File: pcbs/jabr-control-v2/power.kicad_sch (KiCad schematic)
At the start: 0 parts

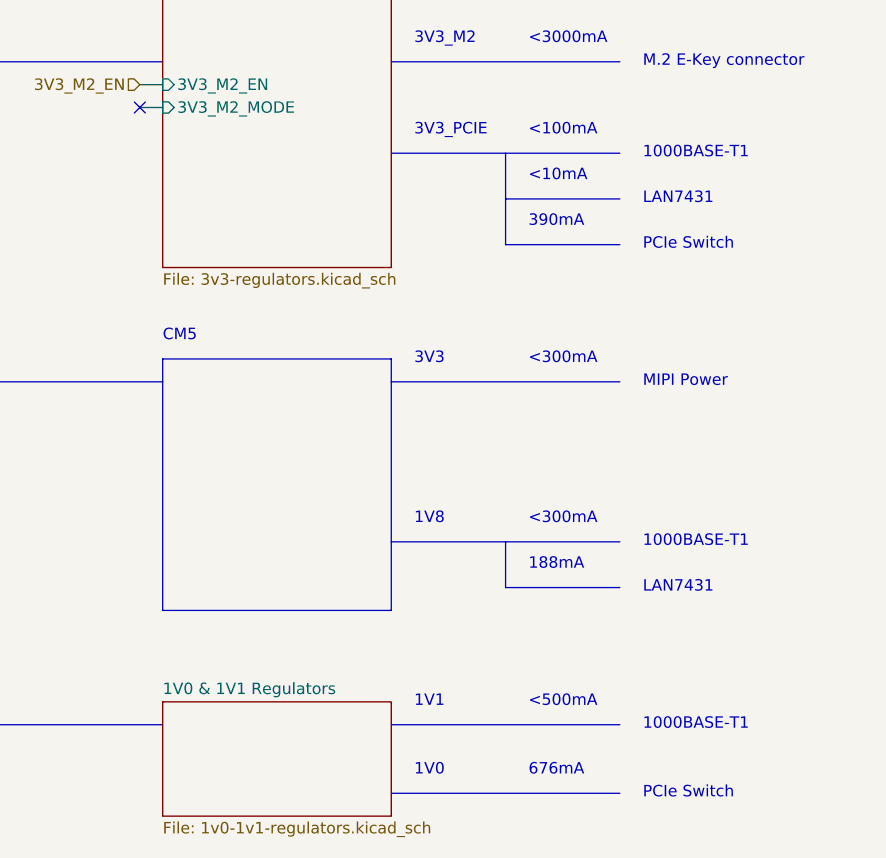
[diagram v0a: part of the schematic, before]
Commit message: PCI11010C Schematic sheet mostly done
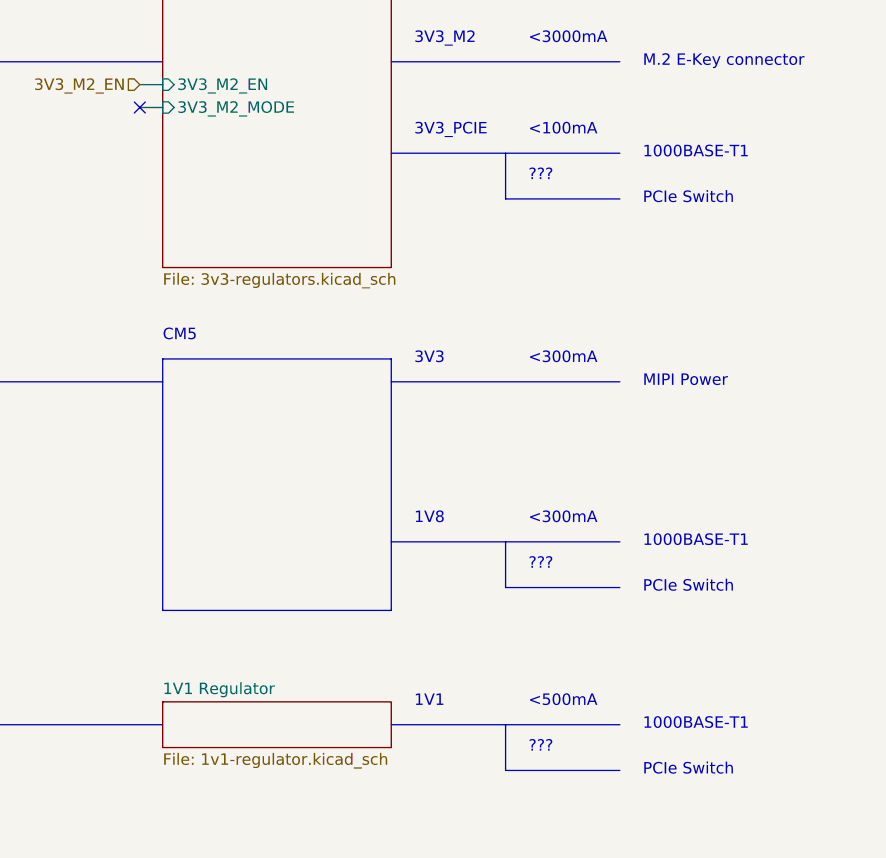
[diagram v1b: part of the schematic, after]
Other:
- sheet 1V0 & 1V1 Regulators renamed 1V1 Regulator
- sheet 1V1 Regulator: file 1v0-1v1-regulators.kicad_sch -> 1v1-regulator.kicad_sch
- note added: "???"
- note removed: "188mA"
- note removed: "1V0"
- note removed: "390mA"
- note removed: "676mA"
- note removed: "<10mA"
- note removed: "LAN7431"
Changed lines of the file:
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@@
 (kicad_sch
-	(version 20250114)
+	(version 20260306)
 	(generator "eeschema")
-	(generator_version "9.0")
+	(generator_version "10.0")
 	(paper "A4")
 	(rectangle
@@
 	(text "PCIe Switch"
 		(exclude_from_sim no)
-		(at 226.06 83.82 0)
-		(effects
-			(font
-				(size 1.27 1.27)
-			)
-			(justify left)
-		)
-	)
-	(text "676mA"
-		(exclude_from_sim no)
-		(at 213.36 142.24 0)
+		(at 226.06 78.74 0)
 		(effects
 			(font
@@
 		)
 	)
-	(text "LAN7431"
+	(text "PCIe Switch"
 		(exclude_from_sim no)
 		(at 226.06 121.92 0)
@@
 		)
 	)
-	(text "188mA"
+	(text "???"
 		(exclude_from_sim no)
 		(at 213.36 119.38 0)
@@
 		)
 	)
-	(text "LAN7431"
-		(exclude_from_sim no)
-		(at 226.06 78.74 0)
+	(text "???"
+		(exclude_from_sim no)
+		(at 213.36 139.7 0)
 		(effects
 			(font
@@
 		)
 	)
-	(text "<10mA"
+	(text "VIN (12V-24V)"
+		(exclude_from_sim no)
+		(at 86.36 43.18 0)
+		(effects
+			(font
+				(size 1.27 1.27)
+			)
+			(justify left)
+		)
+	)
+	(text "<500mA"
+		(exclude_from_sim no)
+		(at 213.36 134.62 0)
+		(effects
+			(font
+				(size 1.27 1.27)
+			)
+			(justify left)
+		)
+	)
+	(text "1V8"
+		(exclude_from_sim no)
+		(at 200.66 114.3 0)
+		(effects
+			(font
+				(size 1.27 1.27)
+			)
+			(justify left)
+		)
+	)
+	(text "<3000mA"
+		(exclude_from_sim no)
+		(at 213.36 60.96 0)
+		(effects
+			(font
+				(size 1.27 1.27)
+			)
+			(justify left)
+		)
+	)
+	(text "1000BASE-T1"
+		(exclude_from_sim no)
+		(at 226.06 73.66 0)
+		(effects
+			(font
+				(size 1.27 1.27)
+			)
+			(justify left)
+		)
+	)
+	(text "<300mA"
+		(exclude_from_sim no)
+		(at 213.36 114.3 0)
+		(effects
+			(font
+				(size 1.27 1.27)
+			)
+			(justify left)
+		)
+	)
+	(text "1000BASE-T1"
+		(exclude_from_sim no)
+		(at 226.06 137.16 0)
+		(effects
+			(font
+				(size 1.27 1.27)
+			)
+			(justify left)
+		)
+	)
+	(text "PCIe Switch"
+		(exclude_from_sim no)
+		(at 226.06 142.24 0)
+		(effects
+			(font
+				(size 1.27 1.27)
+			)
+			(justify left)
+		)
+	)
+	(text "CM5 VBAT"
+		(exclude_from_sim no)
+		(at 226.06 50.8 0)
+		(effects
+			(font
+				(size 1.27 1.27)
+			)
+			(justify left)
+		)
+	)
+	(text "3V3_AON"
+		(exclude_from_sim no)
+		(at 200.66 43.18 0)
+		(effects
+			(font
+				(size 1.27 1.27)
+			)
+			(justify left)
+		)
+	)
+	(text "???"
 		(exclude_from_sim no)
 		(at 213.36 76.2 0)
-		(effects
-			(font
-				(size 1.27 1.27)
-			)
-			(justify left)
-		)
-	)
-	(text "VIN (12V-24V)"
-		(exclude_from_sim no)
-		(at 86.36 43.18 0)
-		(effects
-			(font
-				(size 1.27 1.27)
-			)
-			(justify left)
-		)
-	)
-	(text "<500mA"
-		(exclude_from_sim no)
-		(at 213.36 134.62 0)
-		(effects
-			(font
-				(size 1.27 1.27)
-			)
-			(justify left)
-		)
-	)
-	(text "1V8"
-		(exclude_from_sim no)
-		(at 200.66 114.3 0)
-		(effects
-			(font
-				(size 1.27 1.27)
-			)
-			(justify left)
-		)
-	)
-	(text "<3000mA"
-		(exclude_from_sim no)
-		(at 213.36 60.96 0)
-		(effects
-			(font
-				(size 1.27 1.27)
-			)
-			(justify left)
-		)
-	)
-	(text "1000BASE-T1"
-		(exclude_from_sim no)
-		(at 226.06 73.66 0)
-		(effects
-			(font
-				(size 1.27 1.27)
-			)
-			(justify left)
-		)
-	)
-	(text "<300mA"
-		(exclude_from_sim no)
-		(at 213.36 114.3 0)
-		(effects
-			(font
-				(size 1.27 1.27)
-			)
-			(justify left)
-		)
-	)
-	(text "1000BASE-T1"
-		(exclude_from_sim no)
-		(at 226.06 137.16 0)
-		(effects
-			(font
-				(size 1.27 1.27)
-			)
-			(justify left)
-		)
-	)
-	(text "PCIe Switch"
-		(exclude_from_sim no)
-		(at 226.06 144.78 0)
-		(effects
-			(font
-				(size 1.27 1.27)
-			)
-			(justify left)
-		)
-	)
-	(text "CM5 VBAT"
-		(exclude_from_sim no)
-		(at 226.06 50.8 0)
-		(effects
-			(font
-				(size 1.27 1.27)
-			)
-			(justify left)
-		)
-	)
-	(text "3V3_AON"
-		(exclude_from_sim no)
-		(at 200.66 43.18 0)
-		(effects
-			(font
-				(size 1.27 1.27)
-			)
-			(justify left)
-		)
-	)
-	(text "1V0"
-		(exclude_from_sim no)
-		(at 200.66 142.24 0)
-		(effects
-			(font
-				(size 1.27 1.27)
-			)
-			(justify left)
-		)
-	)
-	(text "390mA"
-		(exclude_from_sim no)
-		(at 213.36 81.28 0)
 		(effects
 			(font
@@
 	(polyline
 		(pts
-			(xy 210.82 78.74) (xy 210.82 83.82)
+			(xy 210.82 78.74) (xy 210.82 78.74)
 		)
 		(stroke
@@
 	(polyline
 		(pts
-			(xy 223.52 83.82) (xy 210.82 83.82)
-		)
-		(stroke
-			(width 0)
-			(type default)
-		)
-	)
-	(polyline
-		(pts
 			(xy 223.52 78.74) (xy 210.82 78.74)
 		)
@@
 	(polyline
 		(pts
+			(xy 210.82 137.16) (xy 210.82 142.24)
+		)
+		(stroke
+			(width 0)
+			(type default)
+		)
+	)
+	(polyline
+		(pts
 			(xy 210.82 116.84) (xy 210.82 121.92)
 		)
@@
 	(polyline
 		(pts
-			(xy 198.12 144.78) (xy 223.52 144.78)
+			(xy 210.82 142.24) (xy 223.52 142.24)
 		)
 		(stroke
@@
 	(sheet
 		(at 172.72 134.62)
-		(size 25.4 12.7)
+		(size 25.4 5.08)
 		(exclude_from_sim no)
 		(in_bom yes)
@@
 		)
 		(fill
-			(color 0 0 0 0.0000)
-		)
-		(property "Sheetname" "1V0 & 1V1 Regulators"
+			(color 0 0 0 0)
+		)
+		(property "Sheetname" "1V1 Regulator"
 			(at 172.72 133.9084 0)
+			(show_name no)
+			(do_not_autoplace no)
 			(effects
 				(font
@@
 			)
 		)
-		(property "Sheetfile" "1v0-1v1-regulators.kicad_sch"
-			(at 172.72 147.9046 0)
+		(property "Sheetfile" "1v1-regulator.kicad_sch"
+			(at 172.72 140.2846 0)
+			(show_name no)
+			(do_not_autoplace no)
 			(effects
 				(font
@@
 		)
 		(instances
-			(project "jabr-control-v1"
+			(project "jabr-control-v2"
 				(path "/f91ec272-d09a-4038-bbbb-962739a92c51/3f551047-3bb0-4f63-99e0-34fd9061d844"
 					(page "15")
@@
 		)
 		(fill
-			(color 0 0 0 0.0000)
+			(color 0 0 0 0)
 		)
 		(property "Sheetname" "3V3 Regulators"
 			(at 172.72 39.9284 0)
+			(show_name no)
+			(do_not_autoplace no)
 			(effects
 				(font
@@
 		(property "Sheetfile" "3v3-regulators.kicad_sch"
 			(at 172.72 86.9446 0)
+			(show_name no)
+			(do_not_autoplace no)
 			(effects
 				(font
@@
 		)
 		(instances
-			(project "jabr-control-v1"
+			(project "jabr-control-v2"
 				(path "/f91ec272-d09a-4038-bbbb-962739a92c51/3f551047-3bb0-4f63-99e0-34fd9061d844"
 					(page "14")
@@
 		)
 		(fill
-			(color 0 0 0 0.0000)
+			(color 0 0 0 0)
 		)
 		(property "Sheetname" "5V Regulator"
 			(at 109.22 60.2484 0)
+			(show_name no)
+			(do_not_autoplace no)
 			(effects
 				(font
@@
 		(property "Sheetfile" "5v-regulator.kicad_sch"
 			(at 109.22 76.7846 0)
+			(show_name no)
+			(do_not_autoplace no)
 			(effects
 				(font
@@
 		)
 		(instances
-			(project "jabr-control-v1"
+			(project "jabr-control-v2"
 				(path "/f91ec272-d09a-4038-bbbb-962739a92c51/3f551047-3bb0-4f63-99e0-34fd9061d844"
 					(page "13")
@@
 		)
 		(fill
-			(color 0 0 0 0.0000)
+			(color 0 0 0 0)
 		)
 		(property "Sheetname" "Power In"
 			(at 58.42 39.9284 0)
+			(show_name no)
+			(do_not_autoplace no)
 			(effects
 				(font
@@
 		(property "Sheetfile" "power-in.kicad_sch"
 			(at 58.42 51.3846 0)
+			(show_name no)
+			(do_not_autoplace no)
 			(effects
 				(font
@@
 		)
 		(instances
-			(project "jabr-control-v1"
+			(project "jabr-control-v2"
 				(path "/f91ec272-d09a-4038-bbbb-962739a92c51/3f551047-3bb0-4f63-99e0-34fd9061d844"
 					(page "12")

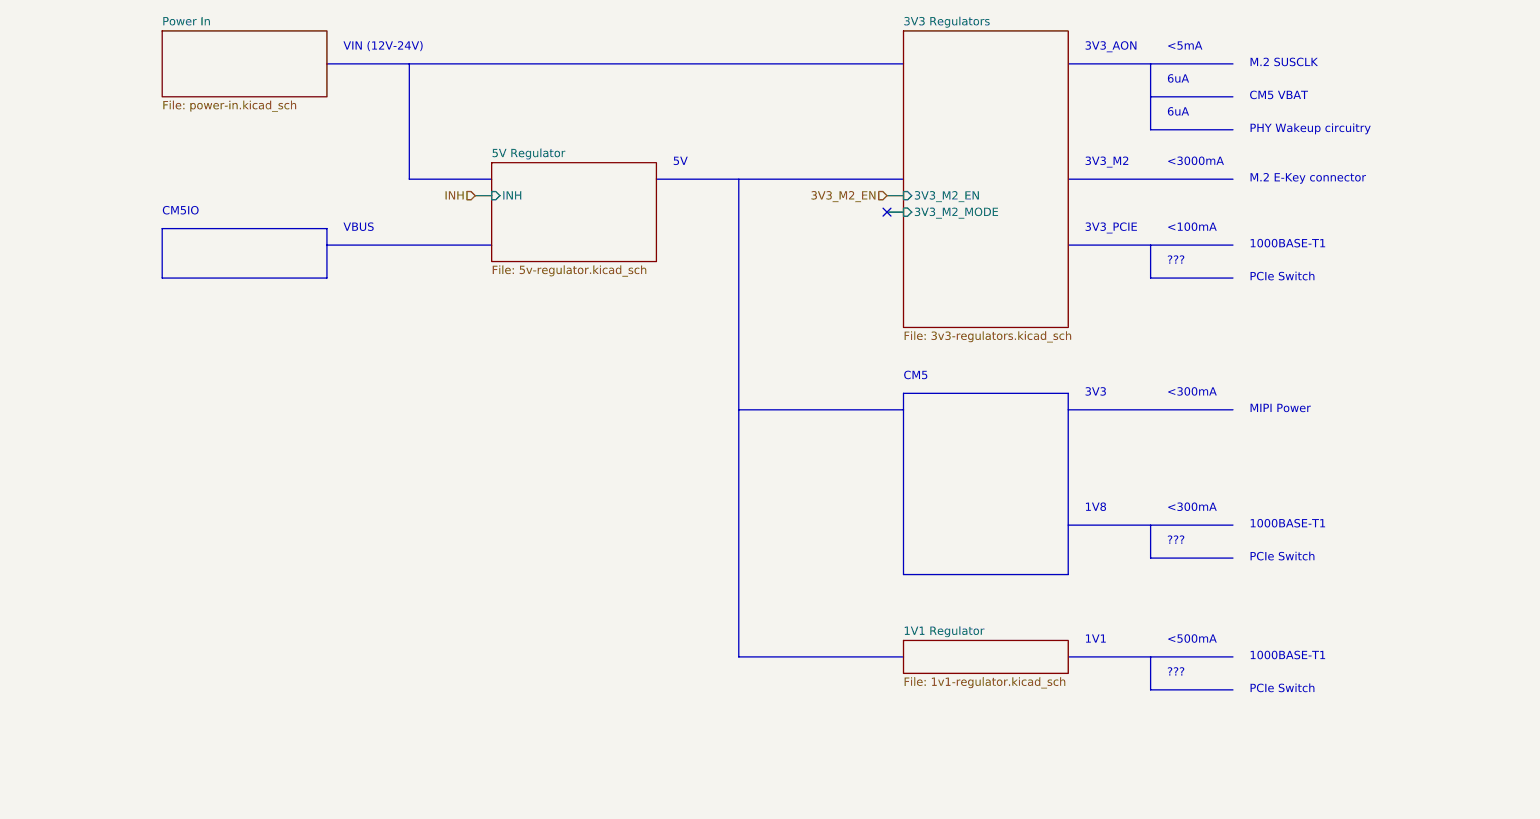
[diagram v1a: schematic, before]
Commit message: Moved M.2 buffers to new sheet
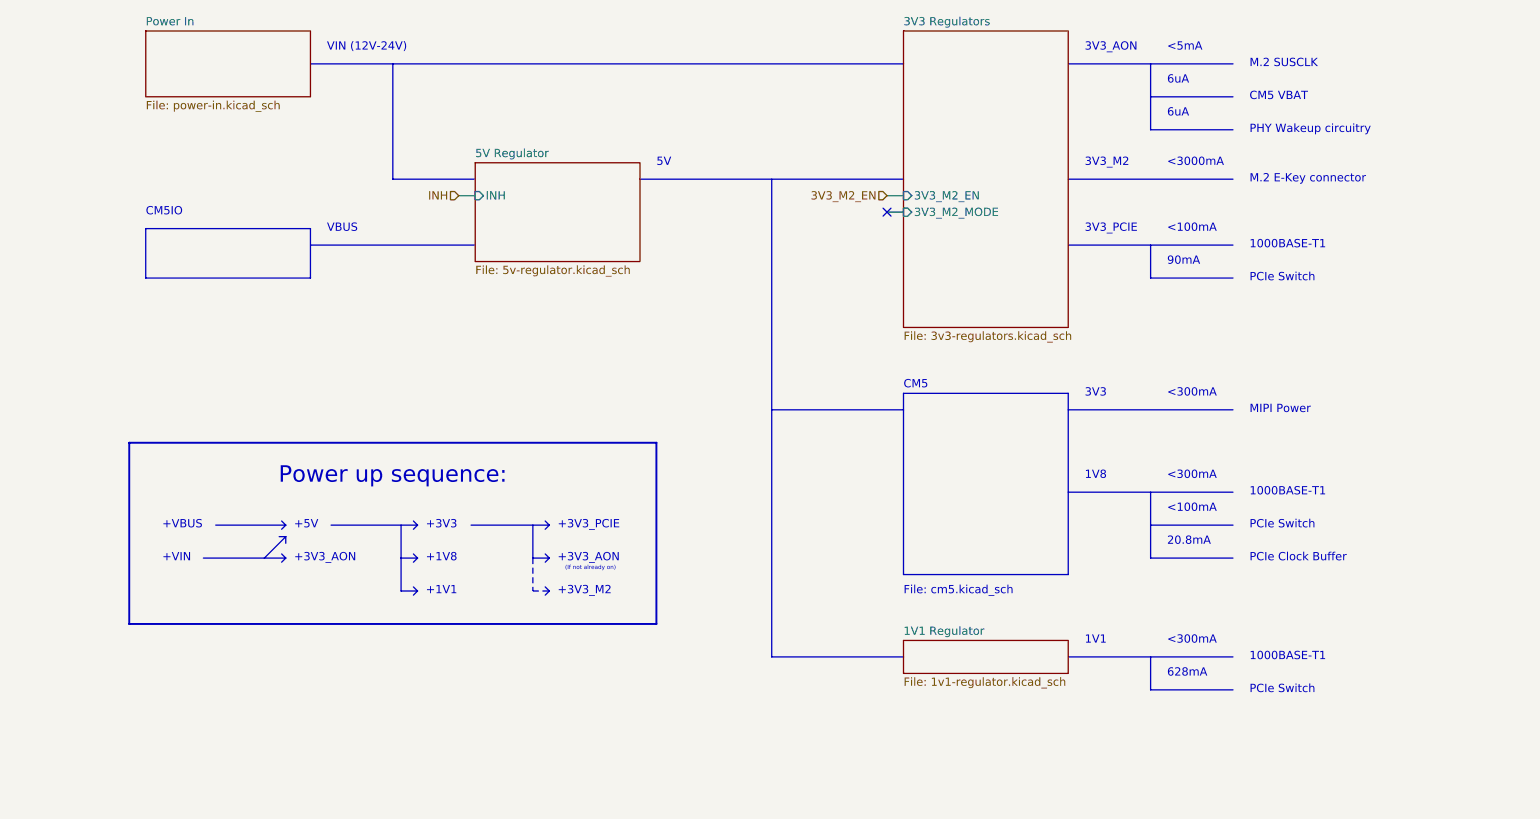
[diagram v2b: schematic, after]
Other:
- note added: "(If not already on)"
- note added: "+1V1"
- note added: "+1V8"
- note added: "+3V3"
- note added: "+3V3_AON"
- note added: "+3V3_M2"
- note added: "+3V3_PCIE"
- note added: "+5V"
- note added: "+VBUS"
- note added: "+VIN"
- note added: "20.8mA"
- note added: "628mA"
- note added: "90mA"
- note added: "File: cm5.kicad_sch"
- note added: "PCIe Clock Buffer"
- note added: "Power up sequence:"
- note removed: "<500mA"
- note removed: "???"

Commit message: Power circuitry done
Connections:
- no-connect marks 1 -> 0
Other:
- sheet 1V1 Regulator renamed PCIe Power
- sheet 3V3 Regulators renamed 3V3 Always On
- sheet 3V3 Always On: file 3v3-regulators.kicad_sch -> 3v3-always-on.kicad_sch
- sheet 3V3 Always On ports: added none; removed 3V3_M2_EN, 3V3_M2_MODE
- sheet PCIe Power: file 1v1-regulator.kicad_sch -> pcie-power.kicad_sch
- sheet PCIe Power ports: added PCIE_EN, PCIE_PG; removed none
- note added: "(Priority)"
- note added: "(η = 85%)"
- note added: "1800mA"
- note added: "1V8_PCIE"
- note added: "5V Select Circuitry"
- note added: "<120uA"
- note added: "<1742mA"
- note added: "<1750mA"
- note added: "<2721mA"
- note added: "<411mA"
- note added: "<421mA"
- note added: "<4900mA"
- note added: "<60uA"
- note added: "<77uA"
- note added: "Control"
- note added: "File: cm5io.kicad_s"
- note added: "Key:"
- note added: "Power"
- note added: "USB-A Ports"
- note removed: "+3V3_M2"
- note removed: "+3V3_PCIE"
- note removed: "3V3_M2"

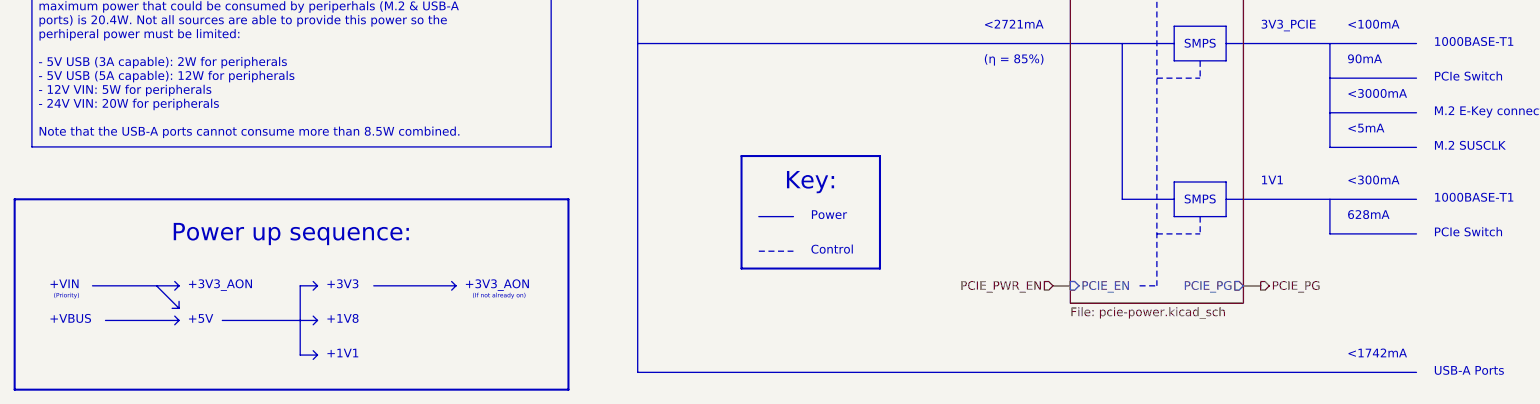
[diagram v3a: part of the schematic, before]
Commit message: Schematic done
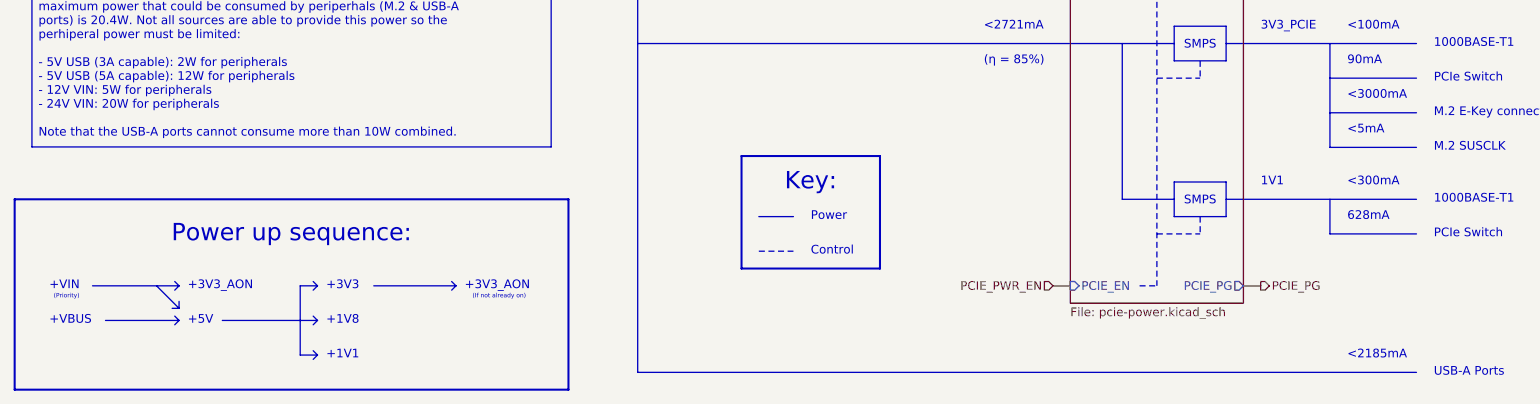
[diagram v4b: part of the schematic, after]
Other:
- note added: "<2185mA"
- note removed: "<1742mA"
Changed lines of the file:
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@@
 			)
 			(justify left top)
-			(href "#10")
+			(href "#8")
 		)
 	)
@@
 		)
 	)
-	(text "<1742mA"
+	(text "<2185mA"
 		(exclude_from_sim no)
 		(at 231.14 154.94 0)
@@
 			)
 			(justify left top)
-			(href "#2")
+			(href "#7")
 		)
 	)
@@
 		)
 	)
-	(text_box "The maximum power that can be consumed by the system is 13W, and the maximum power that could be consumed by periperhals (M.2 & USB-A ports) is 20.4W. Not all sources are able to provide this power so the perhiperal power must be limited:\n\n- 5V USB (3A capable): 2W for peripherals\n- 5V USB (5A capable): 12W for peripherals\n- 12V VIN: 5W for peripherals\n- 24V VIN: 20W for peripherals\n\nNote that the USB-A ports cannot consume more than 8.5W combined."
+	(text_box "The maximum power that can be consumed by the system is 13W, and the maximum power that could be consumed by periperhals (M.2 & USB-A ports) is 20.4W. Not all sources are able to provide this power so the perhiperal power must be limited:\n\n- 5V USB (3A capable): 2W for peripherals\n- 5V USB (5A capable): 12W for peripherals\n- 12V VIN: 5W for peripherals\n- 24V VIN: 20W for peripherals\n\nNote that the USB-A ports cannot consume more than 10W combined."
 		(exclude_from_sim no)
 		(at 38.1 100.0023 0)
@@
 			(project "jabr-control-v2"
 				(path "/f91ec272-d09a-4038-bbbb-962739a92c51/3f551047-3bb0-4f63-99e0-34fd9061d844"
-					(page "15")
+					(page "6")
 				)
 			)
@@
 			(project "jabr-control-v2"
 				(path "/f91ec272-d09a-4038-bbbb-962739a92c51/3f551047-3bb0-4f63-99e0-34fd9061d844"
-					(page "14")
+					(page "5")
 				)
 			)
@@
 			(project "jabr-control-v2"
 				(path "/f91ec272-d09a-4038-bbbb-962739a92c51/3f551047-3bb0-4f63-99e0-34fd9061d844"
-					(page "13")
+					(page "4")
 				)
 			)
@@
 			(project "jabr-control-v2"
 				(path "/f91ec272-d09a-4038-bbbb-962739a92c51/3f551047-3bb0-4f63-99e0-34fd9061d844"
-					(page "12")
+					(page "3")
 				)
 			)
